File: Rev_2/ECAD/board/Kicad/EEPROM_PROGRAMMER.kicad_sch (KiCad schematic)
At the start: 44 parts, among them Q1 PMOS, Q2 PNP, Q3 PNP, Q4 NPN, U1 FT232RL, U2 ATMega328P-AU, U3 ICSP, U4 SD_CARD_READER, U5 SUM, Y1 16MHz

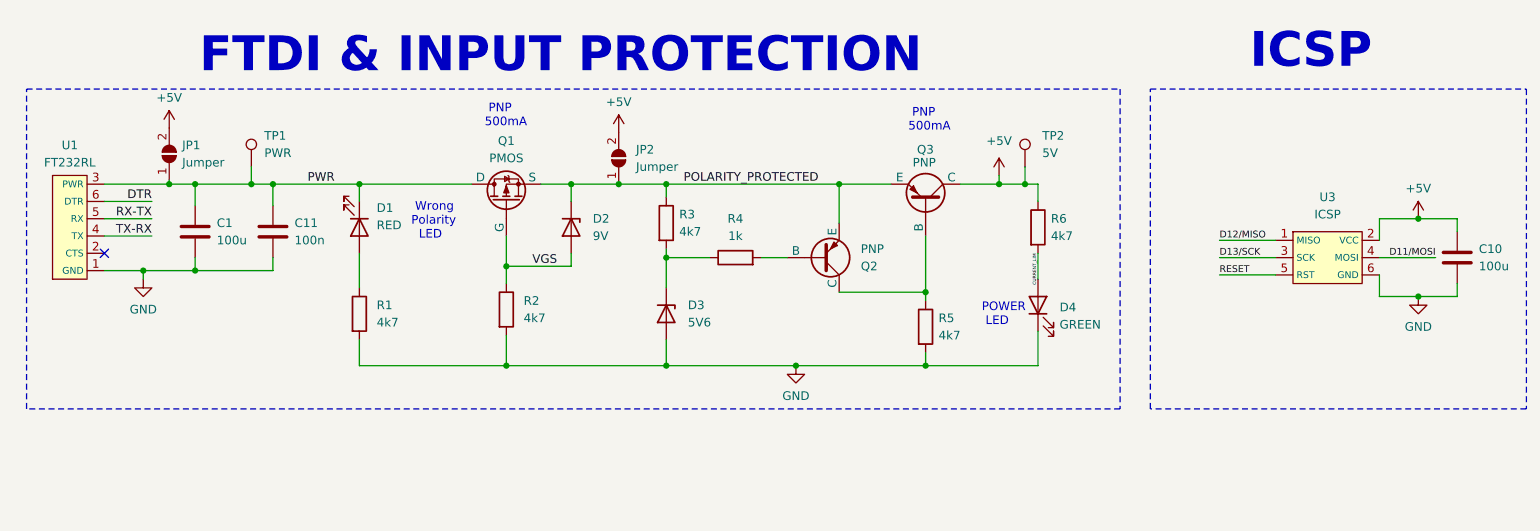
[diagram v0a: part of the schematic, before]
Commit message: Removed overvoltage protection for now
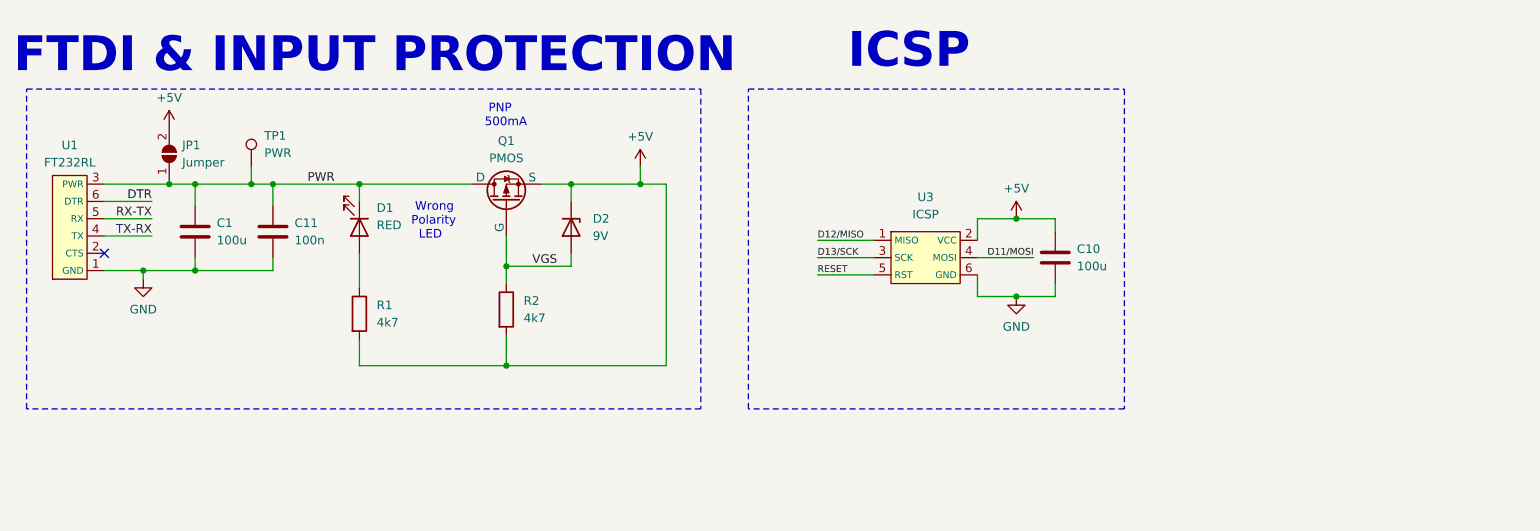
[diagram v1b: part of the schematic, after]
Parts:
- removed D3: 5V6, Diode_THT:D_DO-35_SOD27_P3.81mm_Vertical_AnodeUp, symbol Device:D_Zener
- removed D4: GREEN, LED_SMD:LED_0805_2012Metric_Pad1.15x1.40mm_HandSolder, symbol Device:LED
- removed JP2: Jumper, Jumper:SolderJumper-2_P1.3mm_Open_TrianglePad1.0x1.5mm, symbol Jumper:SolderJumper_2_Open
- removed Q2: PNP, Package_TO_SOT_SMD:SOT-23, symbol Simulation_SPICE:PNP
- removed Q3: PNP, Package_TO_SOT_THT:TO-92, symbol Simulation_SPICE:PNP
- removed R3, R5, R6: 4k7, Resistor_SMD:R_0805_2012Metric_Pad1.20x1.40mm_HandSolder, symbol Device:R
- removed R4: 1k, Resistor_SMD:R_0805_2012Metric_Pad1.20x1.40mm_HandSolder, symbol Device:R
- removed TP2: 5V, symbol Connector:TestPoint
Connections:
- net POLARITY_PROTECTED is gone; now on net +5V: D2.1 (K), Q1.3 (S)
- net +5V: now also R1.2, R2.2
- net GND: no longer R1.2, R2.2
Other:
- note removed: "POWER LED"
- moved on the sheet: C10, U3

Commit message: Ready for PCB-Design
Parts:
- added TP2: GND, TestPoint:TestPoint_Keystone_5005-5009_Compact, symbol Connector:TestPoint
- TP1: footprint (none) -> TestPoint:TestPoint_Keystone_5005-5009_Compact
- renumbered C2 to C10, C3 to C11, C5 to C12, C11 to C2, C10 to C3, C19 to C5, C8 to C6, C6 to C8
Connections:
- net +5V: no longer C3.1, U3.2 (VCC)
- net GND: now also TP2.1
- net PWR renamed POLARITY_PROTECTION
- net POLARITY_PROTECTION: now also C3.1, U3.2 (VCC)
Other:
- moved on the sheet: C3, U3

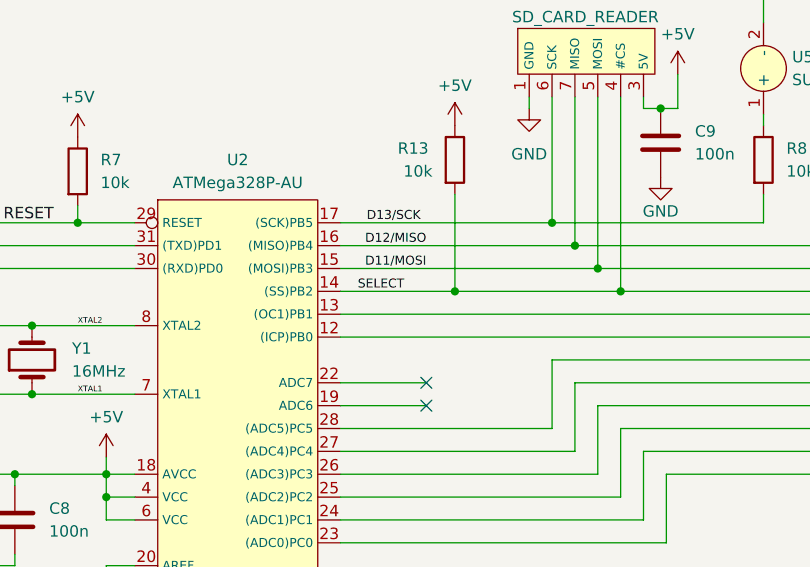
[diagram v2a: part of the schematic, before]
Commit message: Set up bases of board configurations
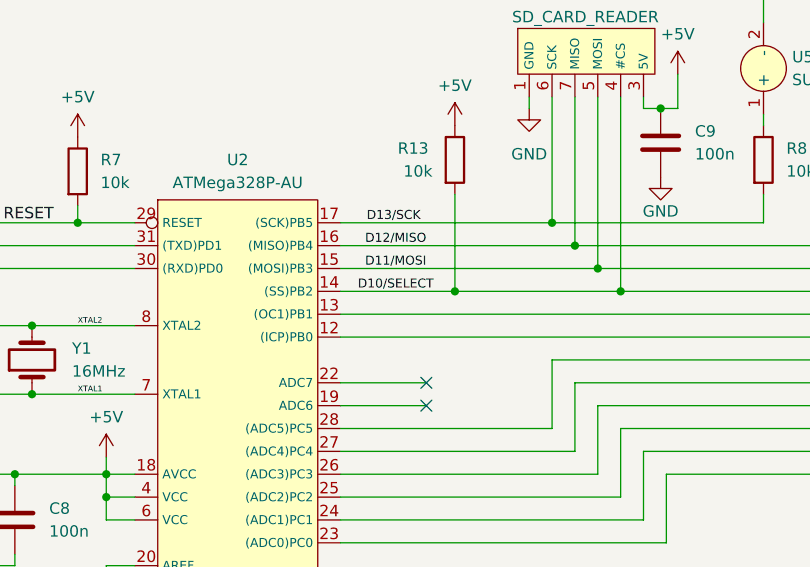
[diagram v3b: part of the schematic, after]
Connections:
- net SELECT renamed D10/SELECT
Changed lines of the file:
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@@
     (effects (font (size 1.27 1.27)) (justify left bottom))
   )
-  (label "SELECT" (at 98.425 155.575 0) (fields_autoplaced)
+  (label "D10{slash}SELECT" (at 98.425 155.575 0) (fields_autoplaced)
     (effects (font (size 1 1)) (justify left bottom))
   )

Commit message: Added missing 3D-models aswell as fixed wrong footprints
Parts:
- C10, C11, C12, C2, C4, C5, C6, C7, C8, C9: footprint Capacitor_THT:CP_Radial_D6.3mm_P2.50mm -> Capacitor_SMD:C_0805_2012Metric_Pad1.18x1.45mm_HandSolder
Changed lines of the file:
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@@
       (effects (font (size 1.27 1.27)) (justify right))
     )
-    (property "Footprint" "Capacitor_THT:CP_Radial_D6.3mm_P2.50mm" (at 59.3598 177.165 0)
+    (property "Footprint" "Capacitor_SMD:C_0805_2012Metric_Pad1.18x1.45mm_HandSolder" (at 59.3598 177.165 0)
       (effects (font (size 1.27 1.27)) hide)
     )
@@
       (effects (font (size 1.27 1.27)))
     )
-    (property "Footprint" "Capacitor_THT:CP_Radial_D6.3mm_P2.50mm" (at 58.42 146.9898 0)
+    (property "Footprint" "Capacitor_SMD:C_0805_2012Metric_Pad1.18x1.45mm_HandSolder" (at 58.42 146.9898 0)
       (effects (font (size 1.27 1.27)) hide)
     )
@@
       (effects (font (size 1.27 1.27)) (justify right))
     )
-    (property "Footprint" "Capacitor_THT:CP_Radial_D6.3mm_P2.50mm" (at 41.5798 177.165 0)
+    (property "Footprint" "Capacitor_SMD:C_0805_2012Metric_Pad1.18x1.45mm_HandSolder" (at 41.5798 177.165 0)
       (effects (font (size 1.27 1.27)) hide)
     )
@@
       (effects (font (size 1.27 1.27)) (justify right))
     )
-    (property "Footprint" "Capacitor_THT:CP_Radial_D6.3mm_P2.50mm" (at 69.5198 187.325 0)
+    (property "Footprint" "Capacitor_SMD:C_0805_2012Metric_Pad1.18x1.45mm_HandSolder" (at 69.5198 187.325 0)
       (effects (font (size 1.27 1.27)) hide)
     )
@@
       (effects (font (size 1.27 1.27)) (justify right))
     )
-    (property "Footprint" "Capacitor_THT:CP_Radial_D6.3mm_P2.50mm" (at 131.1148 135.255 0)
+    (property "Footprint" "Capacitor_SMD:C_0805_2012Metric_Pad1.18x1.45mm_HandSolder" (at 131.1148 135.255 0)
       (effects (font (size 1.27 1.27)) hide)
     )
@@
       (effects (font (size 1.27 1.27)))
     )
-    (property "Footprint" "Capacitor_THT:CP_Radial_D6.3mm_P2.50mm" (at 56.515 166.0398 0)
+    (property "Footprint" "Capacitor_SMD:C_0805_2012Metric_Pad1.18x1.45mm_HandSolder" (at 56.515 166.0398 0)
       (effects (font (size 1.27 1.27)) hide)
     )
@@
       (effects (font (size 1.27 1.27)) (justify left))
     )
-    (property "Footprint" "Capacitor_THT:CP_Radial_D6.3mm_P2.50mm" (at 54.3052 49.53 0)
+    (property "Footprint" "Capacitor_SMD:C_0805_2012Metric_Pad1.18x1.45mm_HandSolder" (at 54.3052 49.53 0)
       (effects (font (size 1.27 1.27)) hide)
     )
@@
       (effects (font (size 1.27 1.27)) (justify right))
     )
-    (property "Footprint" "Capacitor_THT:CP_Radial_D6.3mm_P2.50mm" (at 32.0548 177.165 0)
+    (property "Footprint" "Capacitor_SMD:C_0805_2012Metric_Pad1.18x1.45mm_HandSolder" (at 32.0548 177.165 0)
       (effects (font (size 1.27 1.27)) hide)
     )
@@
       (effects (font (size 1.27 1.27)))
     )
-    (property "Footprint" "Capacitor_THT:CP_Radial_D6.3mm_P2.50mm" (at 56.515 158.4198 0)
+    (property "Footprint" "Capacitor_SMD:C_0805_2012Metric_Pad1.18x1.45mm_HandSolder" (at 56.515 158.4198 0)
       (effects (font (size 1.27 1.27)) hide)
     )
@@
       (effects (font (size 1.27 1.27)) (justify right))
     )
-    (property "Footprint" "Capacitor_THT:CP_Radial_D6.3mm_P2.50mm" (at 50.4698 177.165 0)
-      (effects (font (size 1.27 1.27)) hide)
-    )
+    (property "Footprint" "Capacitor_SMD:C_0805_2012Metric_Pad1.18x1.45mm_HandSolder" (at 50.4698 177.165 0)
+      (effects (font (size 1.27 1.27)) hide)
+    )

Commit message: Done with inital layout
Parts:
- added TP2: 5V, TestPoint:TestPoint_Keystone_5005-5009_Compact, symbol Connector:TestPoint
- renumbered TP2 to TP3
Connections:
- net +5V: now also TP2.1; no longer R1.2, R2.2
- net GND: now also R1.2, R2.2
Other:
- moved on the sheet: C3, TP3, U3
